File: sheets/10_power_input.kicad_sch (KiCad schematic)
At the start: 40 parts, among them J1 MSTBV 2,5/5-GF-5,08, J2 MSTBV 2,5/2-GF-5,08, Q101 STD18NF25, Q102 IPD30N10S3L-34, U101 LM74930QRGERQ1

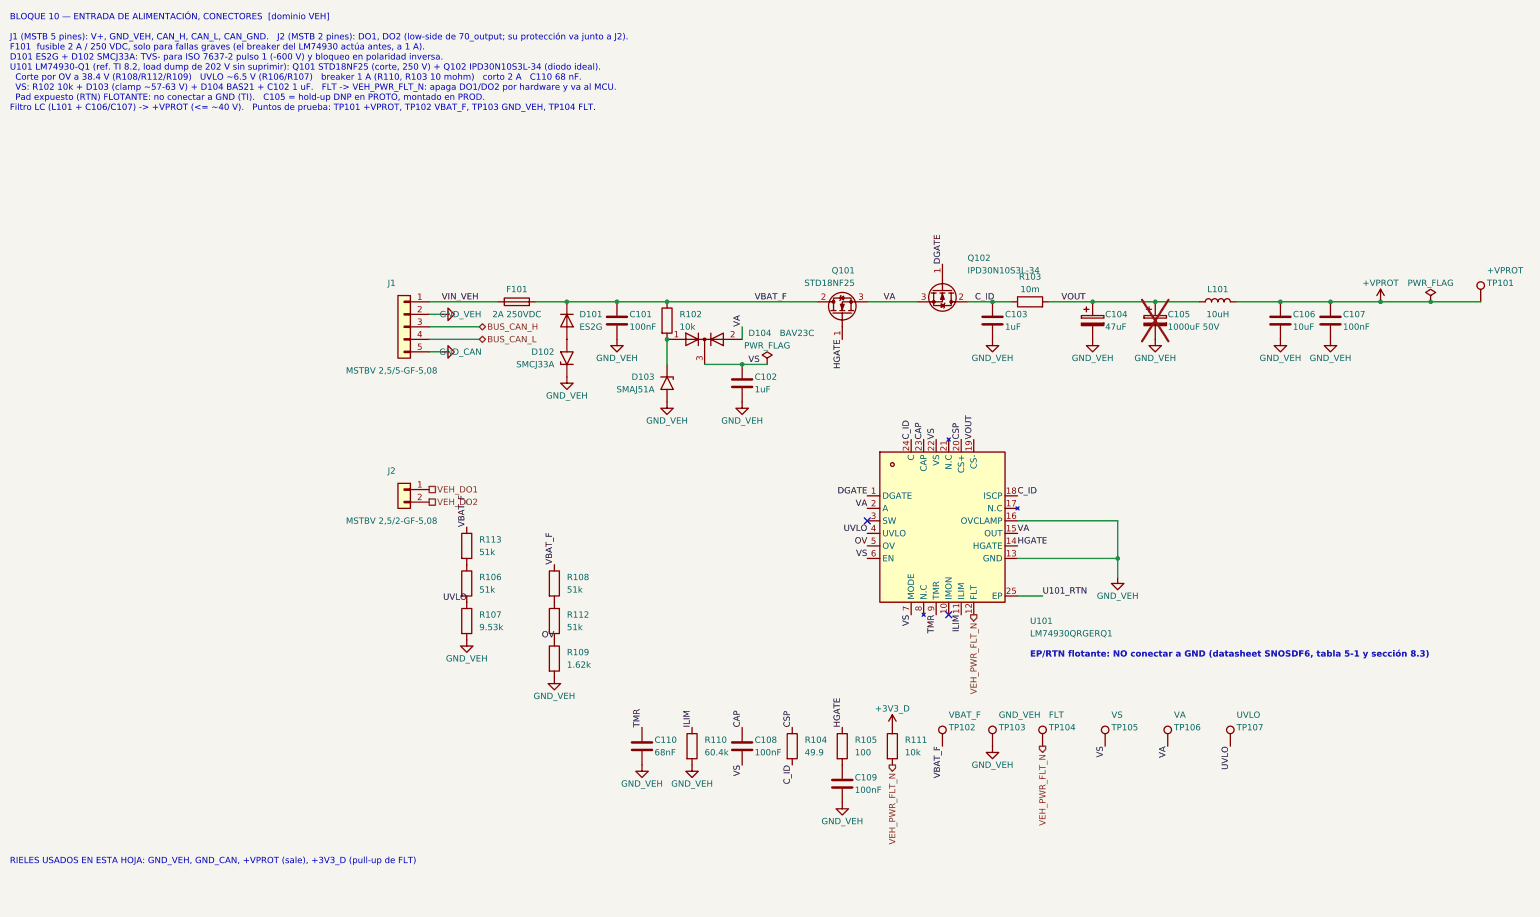
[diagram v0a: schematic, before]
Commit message: update shmatic and serigraphy
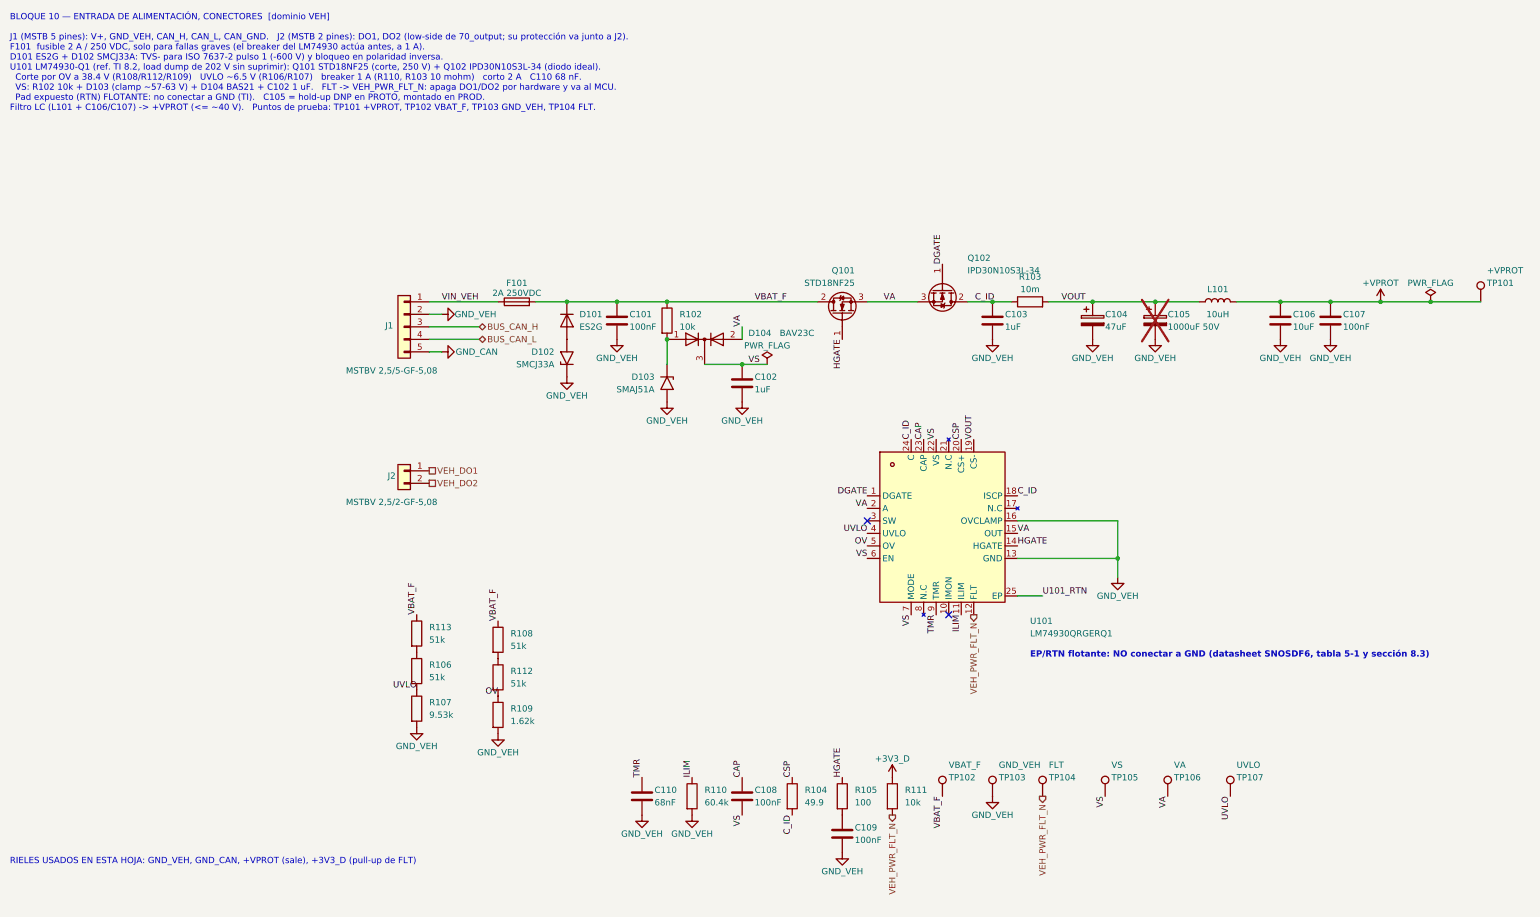
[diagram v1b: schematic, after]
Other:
- moved on the sheet: C108, C109, C110, J2, R104, R105, R106, R107, R108, R109, R110, R111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
